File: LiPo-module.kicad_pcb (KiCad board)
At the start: 2 copper layers, 19 x 26.7 mm, 22 parts, among them J1 USB-C_Power, J2 Conn_01x01_Male, J3 Conn_01x01_Male, J4 Conn_01x01_Male, J5 Conn_01x01_Male, J6 Conn_01x01_Male, J7 Conn_01x01_Male

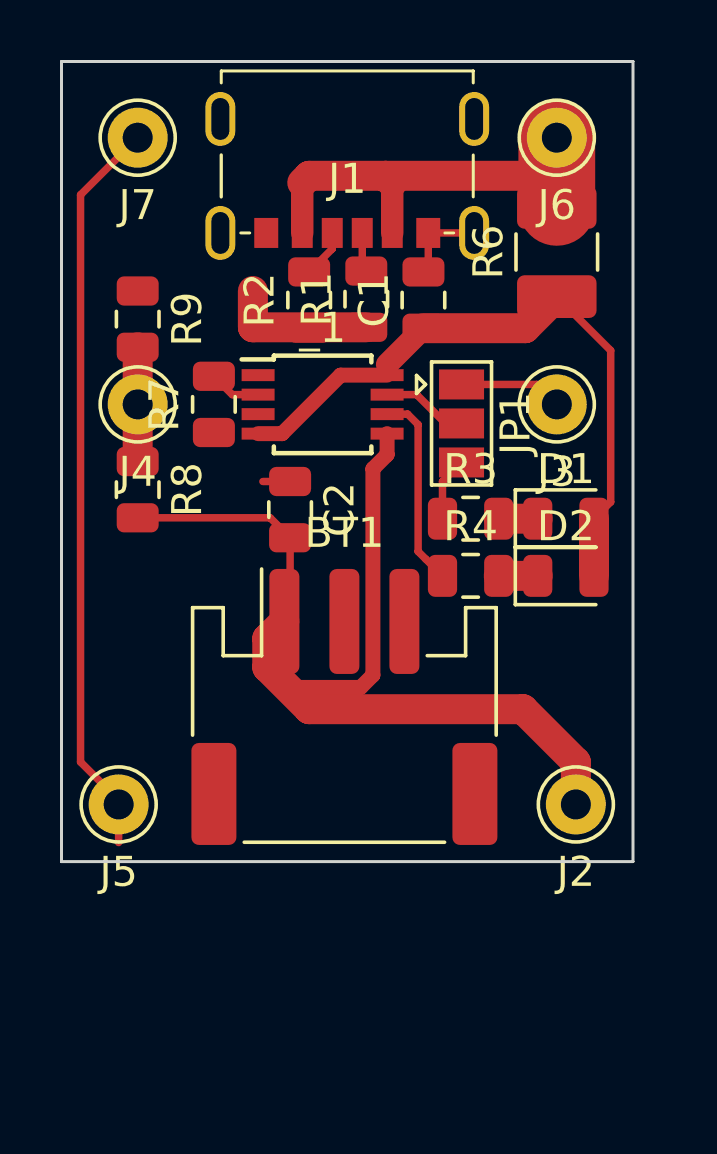
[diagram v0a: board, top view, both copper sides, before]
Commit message: connect ground island
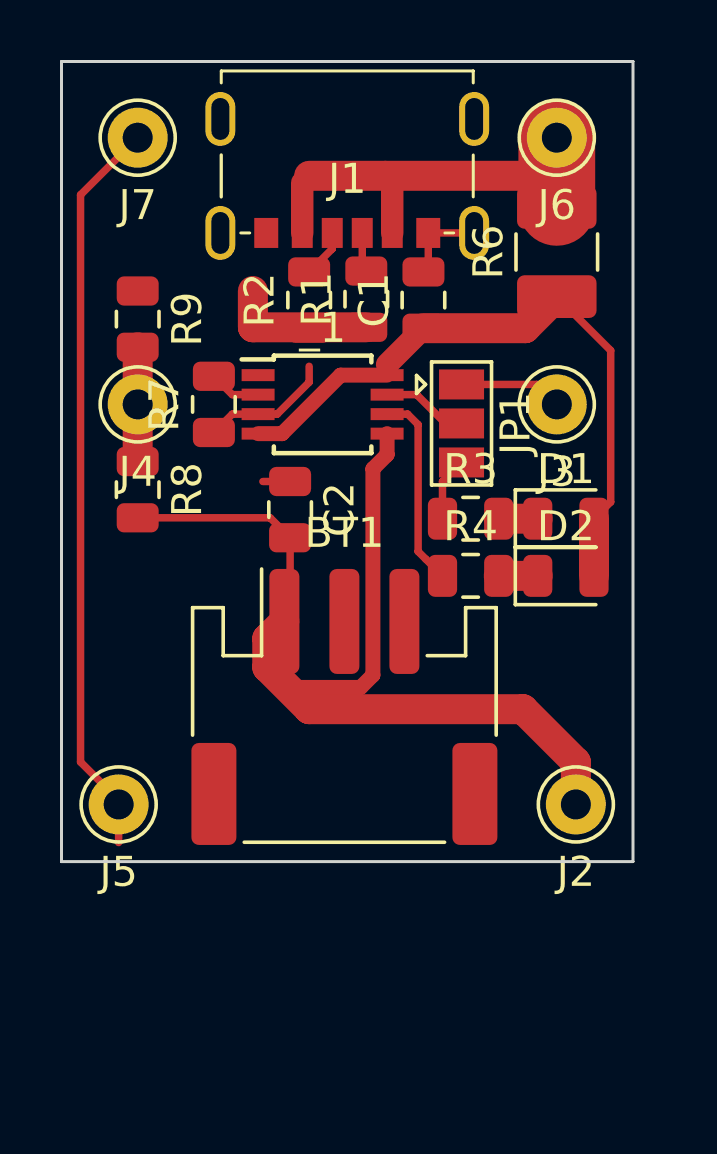
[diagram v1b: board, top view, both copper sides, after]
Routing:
- net GND: track 33.9 -> 38.3 mm
- net +5V: track 14.1 -> 13.4 mm
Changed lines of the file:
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@@
     (thickness 1.6)
     (drawings 4)
-    (tracks 69)
+    (tracks 72)
     (zones 0)
     (modules 22)
@@
   (layers
     (0 F.Cu signal)
-    (31 B.Cu signal)
+    (31 B.Cu signal hide)
     (32 B.Adhes user)
     (33 F.Adhes user)
@@
   )
   (setup
-    (last_trace_width 0.5)
+    (last_trace_width 0.25)
     (user_trace_width 0.5)
     (user_trace_width 0.75)
@@
   (segment (start 165.1 113.520787) (end 165.1 94.615) (width 0.25) (layer F.Cu) (net 1))
   (segment (start 170.845 99.03) (end 170.845 97.82) (width 1) (layer F.Cu) (net 1))
+  (segment (start 171.655214 101.925) (end 172.72 100.860214) (width 0.25) (layer F.Cu) (net 1))
+  (segment (start 171.0184 101.925) (end 171.655214 101.925) (width 0.25) (layer F.Cu) (net 1))
+  (segment (start 172.72 100.860214) (end 172.72 100.33) (width 0.25) (layer F.Cu) (net 1))
+  (segment (start 170.1575 101.925) (end 171.0184 101.925) (width 0.25) (layer F.Cu) (net 1))
+  (segment (start 169.545 102.5375) (end 170.1575 101.925) (width 0.25) (layer F.Cu) (net 1))
   (segment (start 170.1575 101.275) (end 171.0184 101.275) (width 0.25) (layer F.Cu) (net 2))
   (segment (start 169.545 100.6625) (end 170.1575 101.275) (width 0.25) (layer F.Cu) (net 2))
@@
   (segment (start 175.49 95.885) (end 175.49 95.135) (width 0.25) (layer F.Cu) (net 7))
   (segment (start 172.49 95.885) (end 172.49 94.21) (width 0.75) (layer F.Cu) (net 7))
-  (segment (start 172.49 94.21) (end 172.72 93.98) (width 1) (layer F.Cu) (net 7))
   (segment (start 172.72 93.98) (end 175.26 93.98) (width 1) (layer F.Cu) (net 7))
   (segment (start 175.49 94.21) (end 175.49 95.885) (width 0.75) (layer F.Cu) (net 7))
-  (segment (start 175.26 93.98) (end 175.49 94.21) (width 1) (layer F.Cu) (net 7))
   (segment (start 175.26 93.98) (end 179.705 93.98) (width 1) (layer F.Cu) (net 7))
   (segment (start 180.975 95.0325) (end 180.975 92.71) (width 2.56) (layer F.Cu) (net 7))

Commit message: add lipo protection to schematic
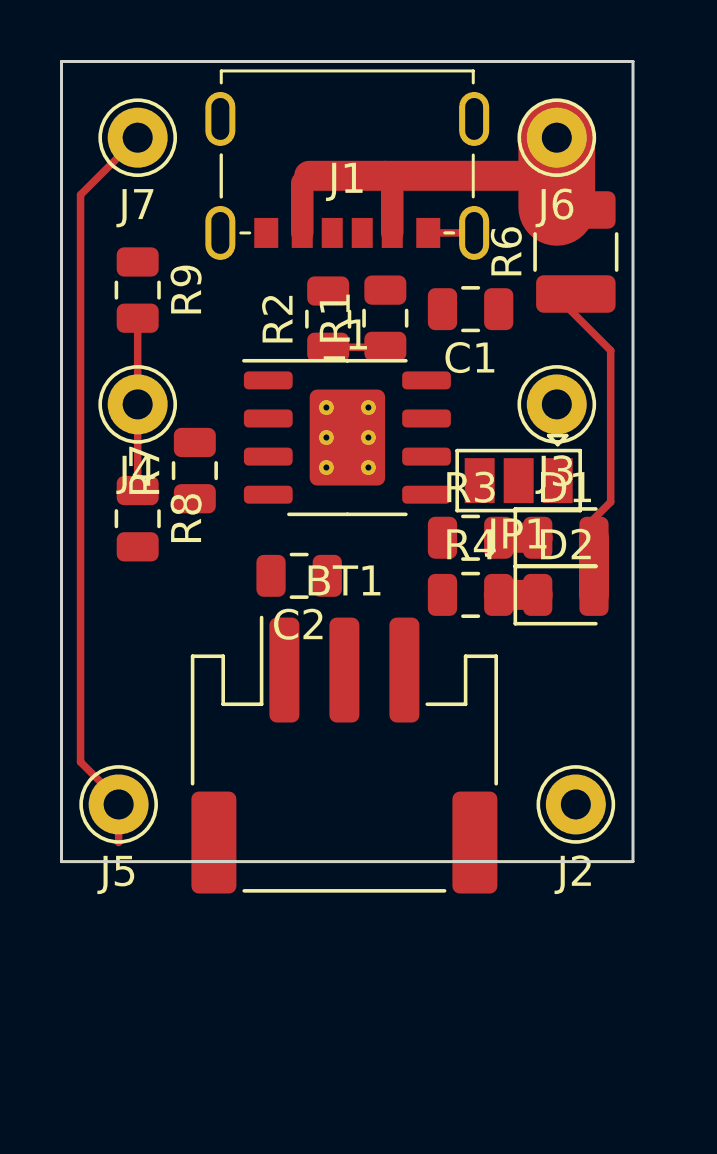
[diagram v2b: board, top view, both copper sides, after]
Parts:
- R6: footprint Resistor_SMD:R_1210_3225Metric_Pad1.42x2.65mm_HandSolder -> Resistor_SMD:R_1210_3225Metric
- _1: footprint parts:TP4056 -> Package_SO:SOIC-8-1EP_3.9x4.9mm_P1.27mm_EP2.514x3.2mm_ThermalVias
- moved JP1 2.69 mm to (179.7, 104.1), turned to 180 degrees
- moved R7 2.30 mm to (168.9, 103.8)
- moved C2 2.23 mm to (172.4, 107.3), turned to 180 degrees
- moved BT1 1.62 mm to (173.9, 113.3)
- moved C1 1.60 mm to (178.1, 98.4), turned to 180 degrees
- moved _1 1.38 mm to (174.0, 102.7)
- moved R8 0.97 mm to (167.0, 105.4)
- moved R9 0.97 mm to (167.0, 97.8)
- moved R1 0.90 mm to (175.3, 98.7)
- moved R2 0.90 mm to (173.4, 98.8)
- moved R6 0.64 mm to (181.6, 96.5)
- moved D1 0.64 mm to (181.3, 106.0)
- moved D2 0.64 mm to (181.3, 108.0)
- moved R3 0.64 mm to (178.1, 106.0)
- moved R4 0.64 mm to (178.1, 108.0)
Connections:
- BT1 pad MP: GND -> (no net)
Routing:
- net /vBAT: track 36.4 -> 0.27 mm
- net Net-(C1-Pad1): track 22.3 -> 10.3 mm
- net GND: track 38.3 -> 28.3 mm
- net Net-(R4-Pad1): track 6.56 -> 0.00 mm
- net /CHARGING: track 3.45 -> 0.00 mm
- net Net-(JP1-Pad2): track 2.88 -> 0.00 mm
- net Net-(JP1-Pad3): track 2.14 -> 0.00 mm
- net /BATTERY: track 3.81 -> 5.74 mm
- net Net-(R7-Pad2): track 1.73 -> 0.00 mm
- net Net-(J1-Pad4): track 1.62 -> 0.00 mm
- net Net-(J1-Pad3): track 1.33 -> 0.19 mm

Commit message: add lipo protection circuitry
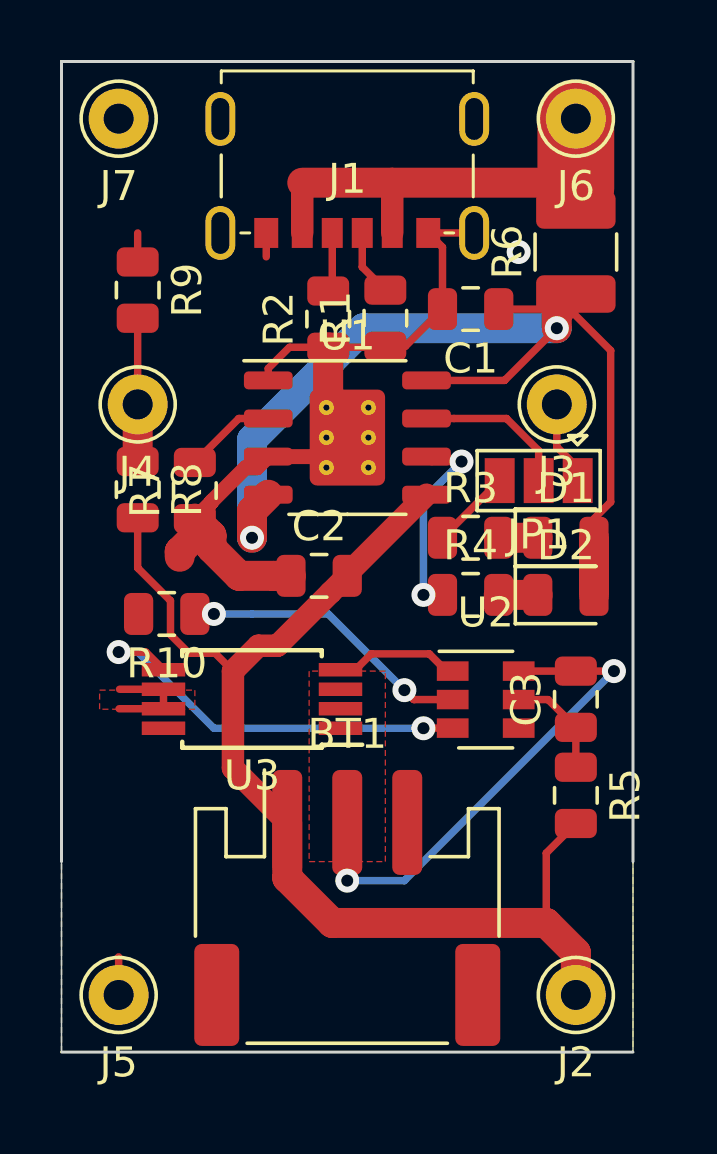
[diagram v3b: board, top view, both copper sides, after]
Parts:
- added C3: 0.1uF, Capacitor_SMD:C_0805_2012Metric, F.Cu at (181.6, 111.4)
- added R10: 2K, Resistor_SMD:R_0805_2012Metric, F.Cu at (168.0, 108.6)
- added R5: 470, Resistor_SMD:R_0805_2012Metric, F.Cu at (181.6, 114.6)
- added U2: DW01A, Package_TO_SOT_SMD:SOT-23-6, F.Cu at (178.6, 111.4)
- added U3: FS8205A, Package_SO:TSSOP-8_4.4x3mm_P0.65mm, F.Cu at (170.8, 111.4)
- moved J2 6.35 mm to (181.6, 121.3)
- moved J5 6.35 mm to (166.4, 121.3)
- moved BT1 5.08 mm to (174.0, 118.4)
- moved R8 0.97 mm to (167.0, 104.4)
- moved J6 0.90 mm to (181.6, 92.1)
- moved J7 0.90 mm to (166.4, 92.1)
- moved C2 0.67 mm to (173.1, 107.3), turned to 0 degrees
- moved JP1 0.66 mm to (180.4, 104.1)
- moved R7 0.66 mm to (168.9, 104.5)
- renumbered _1 to U1
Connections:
- BT1 pad 2: GND -> /BAT_GND
- BT1 pad MP: (no net) -> GND
- U1 pad 9: (no net) -> GND
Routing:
- net /vBAT: track 0.27 -> 39.3 mm
- net Net-(C1-Pad1): track 10.3 -> 36.2 mm, vias 0 -> 2
- net /BAT_GND: track 0.00 -> 17.7 mm, vias 0 -> 2
- net /OC: track 0.00 -> 13.9 mm, vias 0 -> 2
- net /CS: track 0.00 -> 9.78 mm, vias 0 -> 2
- net Net-(R4-Pad1): track 0.00 -> 6.84 mm, vias 0 -> 2
- net GND: track 28.3 -> 34.2 mm, vias 0 -> 1
- net Net-(JP1-Pad2): track 0.00 -> 5.18 mm
- net /OD: track 0.00 -> 4.32 mm
- net /vcc: track 0.00 -> 3.62 mm
- net Net-(R7-Pad2): track 0.00 -> 3.05 mm
- net /CHARGING: track 0.00 -> 2.83 mm
- net Net-(JP1-Pad3): track 0.00 -> 2.69 mm
- net Net-(J1-Pad3): track 0.19 -> 2.41 mm
- net +5V: track 13.4 -> 15.6 mm
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- added copper zone on F.Cu, net /BAT_GND
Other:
- board size 19 x 26.7 mm -> 19 x 33 mm
